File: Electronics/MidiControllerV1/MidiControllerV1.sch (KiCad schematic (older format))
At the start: 47 parts

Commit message: #2 Schematic wired up
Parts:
- removed C? (x2): C, symbol Device:C
- removed Y?: Crystal, symbol Device:Crystal
- added J?: Conn_01x04_Female, symbol Connector:Conn_01x04_Female
- J?: value Conn_01x03_Female -> BOOT1_JUMPER
- J?: value Conn_01x03_Female -> BOOT0_JUMPER
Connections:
- net labels added: +3.3V, +5V, BOOT0, BOOT1, ENCA, ENCB, ENC_SW, GND, KP_C1, KP_C2, KP_C3, KP_C4, KP_R1, KP_R2, KP_R3, KP_R4, LCD_SCL, LCD_SDA, OSCIN, OSCOUT, SR_CLK, SR_DATA, SR_LATCH, SWDCLK, SWDIO, USBD+, USBD-
- wire segments 0 -> 106
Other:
- moved on the sheet: C?, D?, J?, R?, SW?, U?, Y?

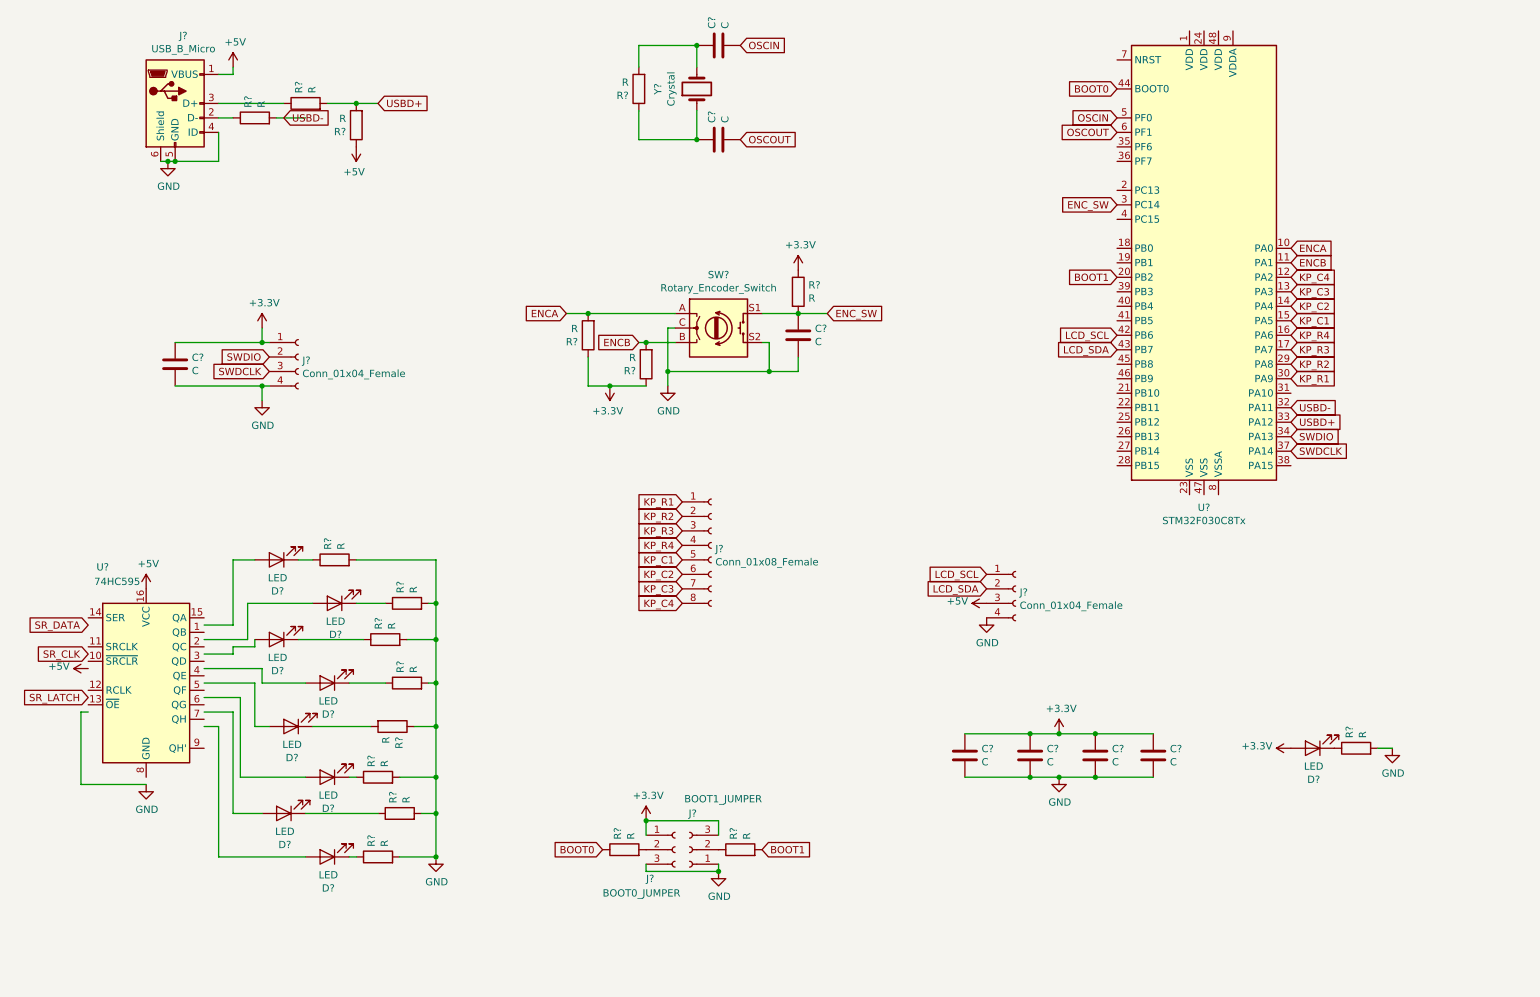
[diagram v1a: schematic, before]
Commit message: Updated schematic
Schematic updated to use blue pill board plugged into headers
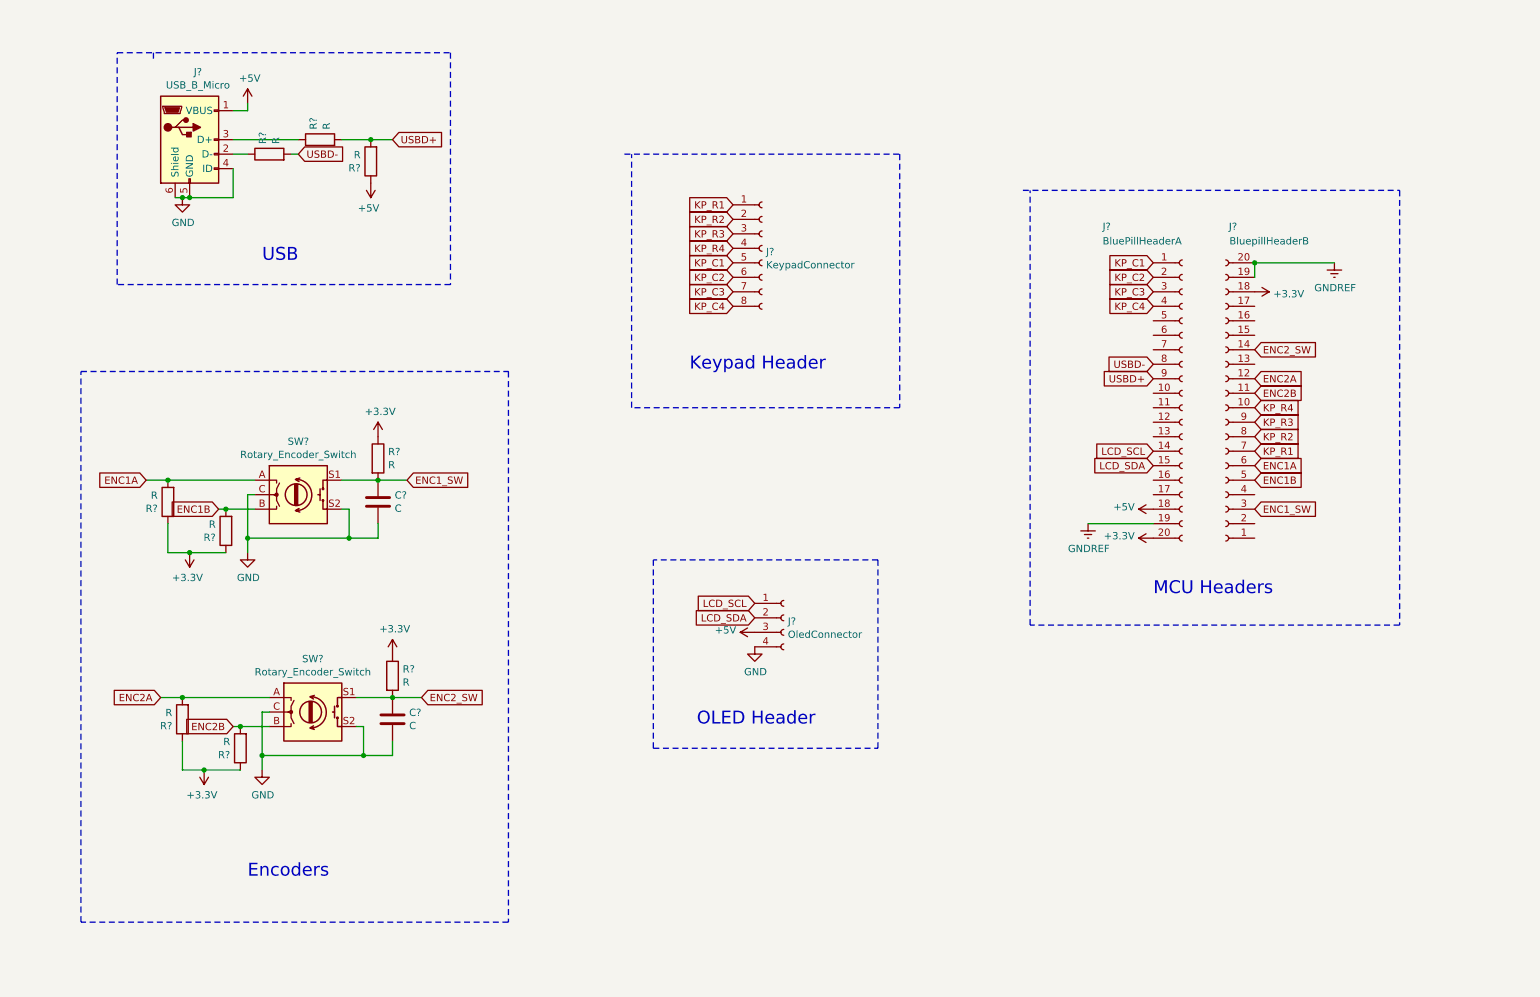
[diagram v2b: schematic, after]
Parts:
- removed C? (x7): C, symbol Device:C
- removed D? (x9): LED, symbol Device:LED
- removed J?: Conn_01x04_Female, symbol Connector:Conn_01x04_Female
- removed J?: BOOT1_JUMPER, symbol Connector:Conn_01x03_Female
- removed J?: BOOT0_JUMPER, symbol Connector:Conn_01x03_Female
- removed R? (x12): R, symbol Device:R
- removed U?: STM32F030C8Tx, Package_QFP:LQFP-48_7x7mm_P0.5mm, symbol MCU_ST_STM32F0:STM32F030C8Tx
- removed U?: 74HC595, symbol 74xx:74HC595
- removed Y?: Crystal, symbol Device:Crystal
- added C?: C, symbol Device:C
- added J?: BluePillHeaderA, symbol Connector:Conn_01x20_Female
- added J?: BluepillHeaderB, symbol Connector:Conn_01x20_Female
- added R? (x3): R, symbol Device:R
- added SW?: Rotary_Encoder_Switch, symbol Device:Rotary_Encoder_Switch
- J?: value Conn_01x08_Female -> KeypadConnector
- J?: value Conn_01x04_Female -> OledConnector
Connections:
- net labels added: ENC1A, ENC1B, ENC1_SW, ENC2A, ENC2B, ENC2_SW, GNDREF
- net labels removed: BOOT0, BOOT1, ENCA, ENCB, ENC_SW, OSCIN, OSCOUT, SR_CLK, SR_DATA, SR_LATCH, SWDCLK, SWDIO
- wire segments 106 -> 48
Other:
- note added: "Encoders\n"
- note added: "Keypad Header\n"
- note added: "MCU Headers"
- note added: "OLED Header"
- note added: "USB"
- moved on the sheet: C?, J?, R?, SW?

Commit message: Components placed on pcb
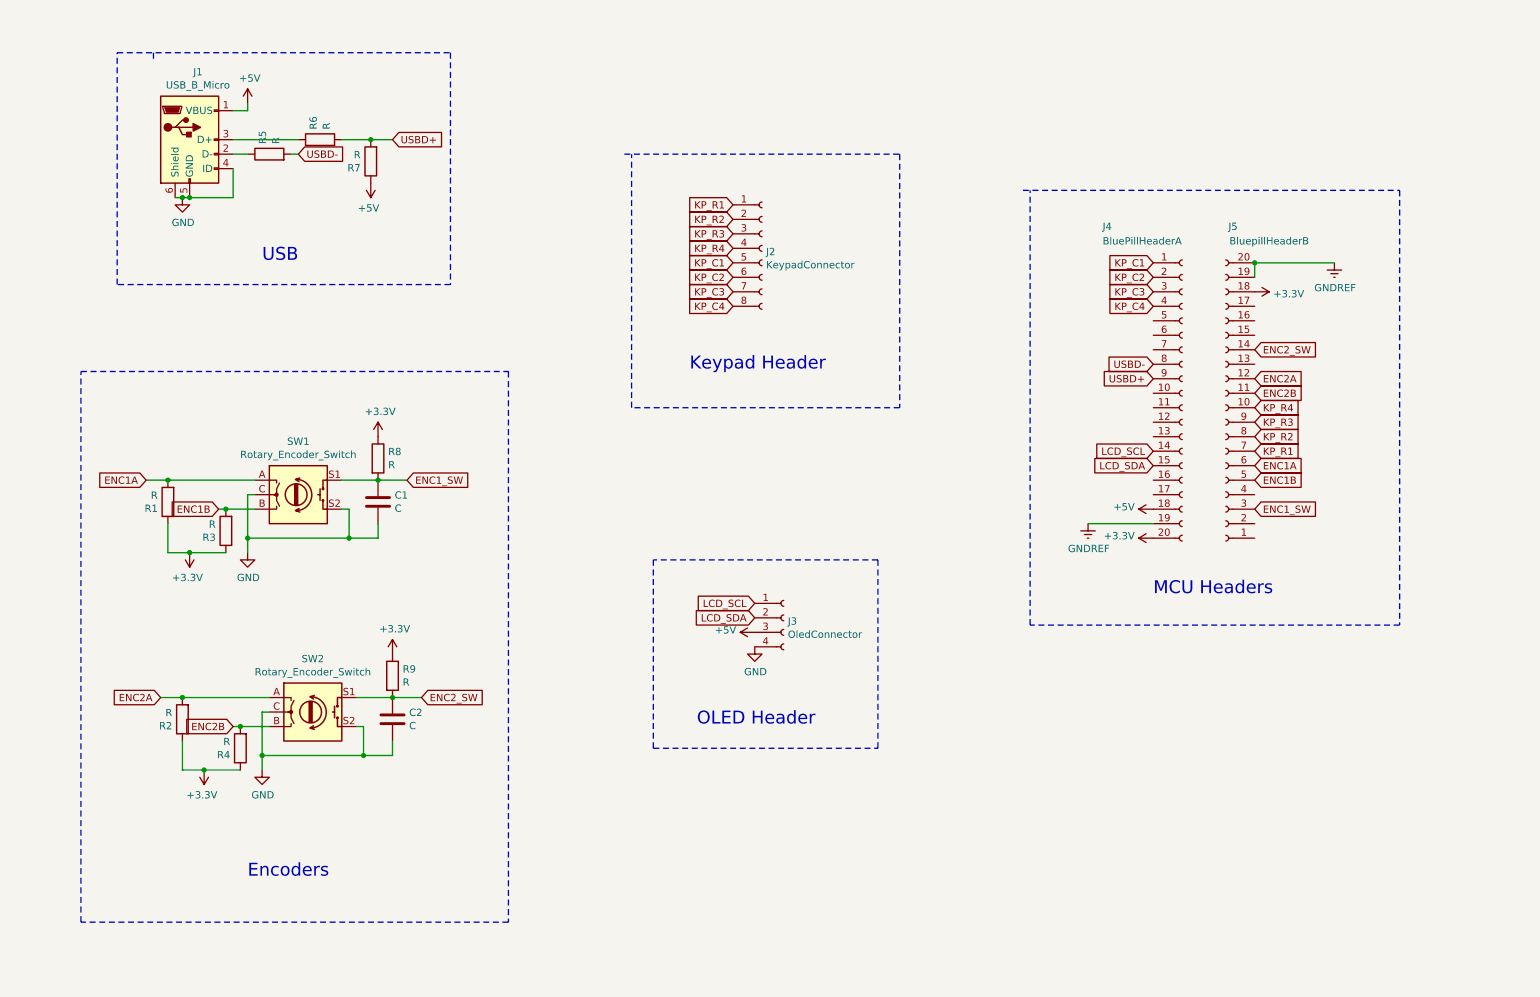
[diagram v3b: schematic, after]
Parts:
- J1: renamed from J?; footprint (none) -> Connector_USB:USB_Micro-B_Molex-105017-0001
- J2: renamed from J?; footprint (none) -> Connector_PinHeader_2.54mm:PinHeader_1x06_P2.54mm_Vertical
- J3: renamed from J?; footprint (none) -> Connector_PinHeader_2.54mm:PinHeader_1x04_P2.54mm_Vertical
- J4, J5: renamed from J?; footprint (none) -> Connector_PinHeader_2.54mm:PinHeader_1x20_P2.54mm_Vertical
- R1, R2, R3, R4, R5, R6, R7, R8, R9: renamed from R?; footprint (none) -> Resistor_SMD:R_1206_3216Metric
- SW1, SW2: renamed from SW?; footprint (none) -> Rotary_Encoder:RotaryEncoder_Alps_EC11E-Switch_Vertical_H20mm
- gave numbers to parts that had none: 2

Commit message: #25 Sequencer note selection kind of working
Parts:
- C1, C2: footprint (none) -> Capacitor_THT:C_Disc_D5.1mm_W3.2mm_P5.00mm
- J2: footprint Connector_PinHeader_2.54mm:PinHeader_1x06_P2.54mm_Vertical -> Connector_PinHeader_2.54mm:PinHeader_1x08_P2.54mm_Vertical
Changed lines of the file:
@@
 F 0 "J2" H 5928 2376 50  0000 L CNN
 F 1 "KeypadConnector" H 5928 2285 50  0000 L CNN
-F 2 "Connector_PinHeader_2.54mm:PinHeader_1x06_P2.54mm_Vertical" H 5900 2400 50  0001 C CNN
+F 2 "Connector_PinHeader_2.54mm:PinHeader_1x08_P2.54mm_Vertical" H 5900 2400 50  0001 C CNN
 F 3 "~" H 5900 2400 50  0001 C CNN
 	1    5900 2400
@@
 F 0 "C1" H 3365 4196 50  0000 L CNN
 F 1 "C" H 3365 4105 50  0000 L CNN
-F 2 "" H 3288 4000 50  0001 C CNN
+F 2 "Capacitor_THT:C_Disc_D5.1mm_W3.2mm_P5.00mm" H 3288 4000 50  0001 C CNN
 F 3 "~" H 3250 4150 50  0001 C CNN
 	1    3250 4150
@@
 F 0 "C2" H 3465 5696 50  0000 L CNN
 F 1 "C" H 3465 5605 50  0000 L CNN
-F 2 "" H 3388 5500 50  0001 C CNN
+F 2 "Capacitor_THT:C_Disc_D5.1mm_W3.2mm_P5.00mm" H 3388 5500 50  0001 C CNN
 F 3 "~" H 3350 5650 50  0001 C CNN
 	1    3350 5650

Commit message: #32 Updated pcb v1
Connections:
- net LCD_SCL: now also J3.2 (Pin_2); no longer J3.1 (Pin_1)
- net LCD_SDA: now also J3.1 (Pin_1); no longer J3.2 (Pin_2)
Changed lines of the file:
@@
 	0    -1   -1   0
 $EndComp
+Text GLabel 5850 4850 0    50   Input ~ 0
+LCD_SDA
 Text GLabel 5850 4950 0    50   Input ~ 0
-LCD_SDA
-Text GLabel 5850 4850 0    50   Input ~ 0
 LCD_SCL
 Text GLabel 8600 3900 0    50   Input ~ 0
